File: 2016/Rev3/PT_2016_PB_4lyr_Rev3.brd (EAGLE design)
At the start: 155.7 x 202.7 mm, 170 parts, among them Q1 MOSFET-NCHANNELFDD8780, Q12 2N7002, Q3 MOSFET-NCHANNELFDD8780, Q4 MMBT2222A, Q5 MMBT4403

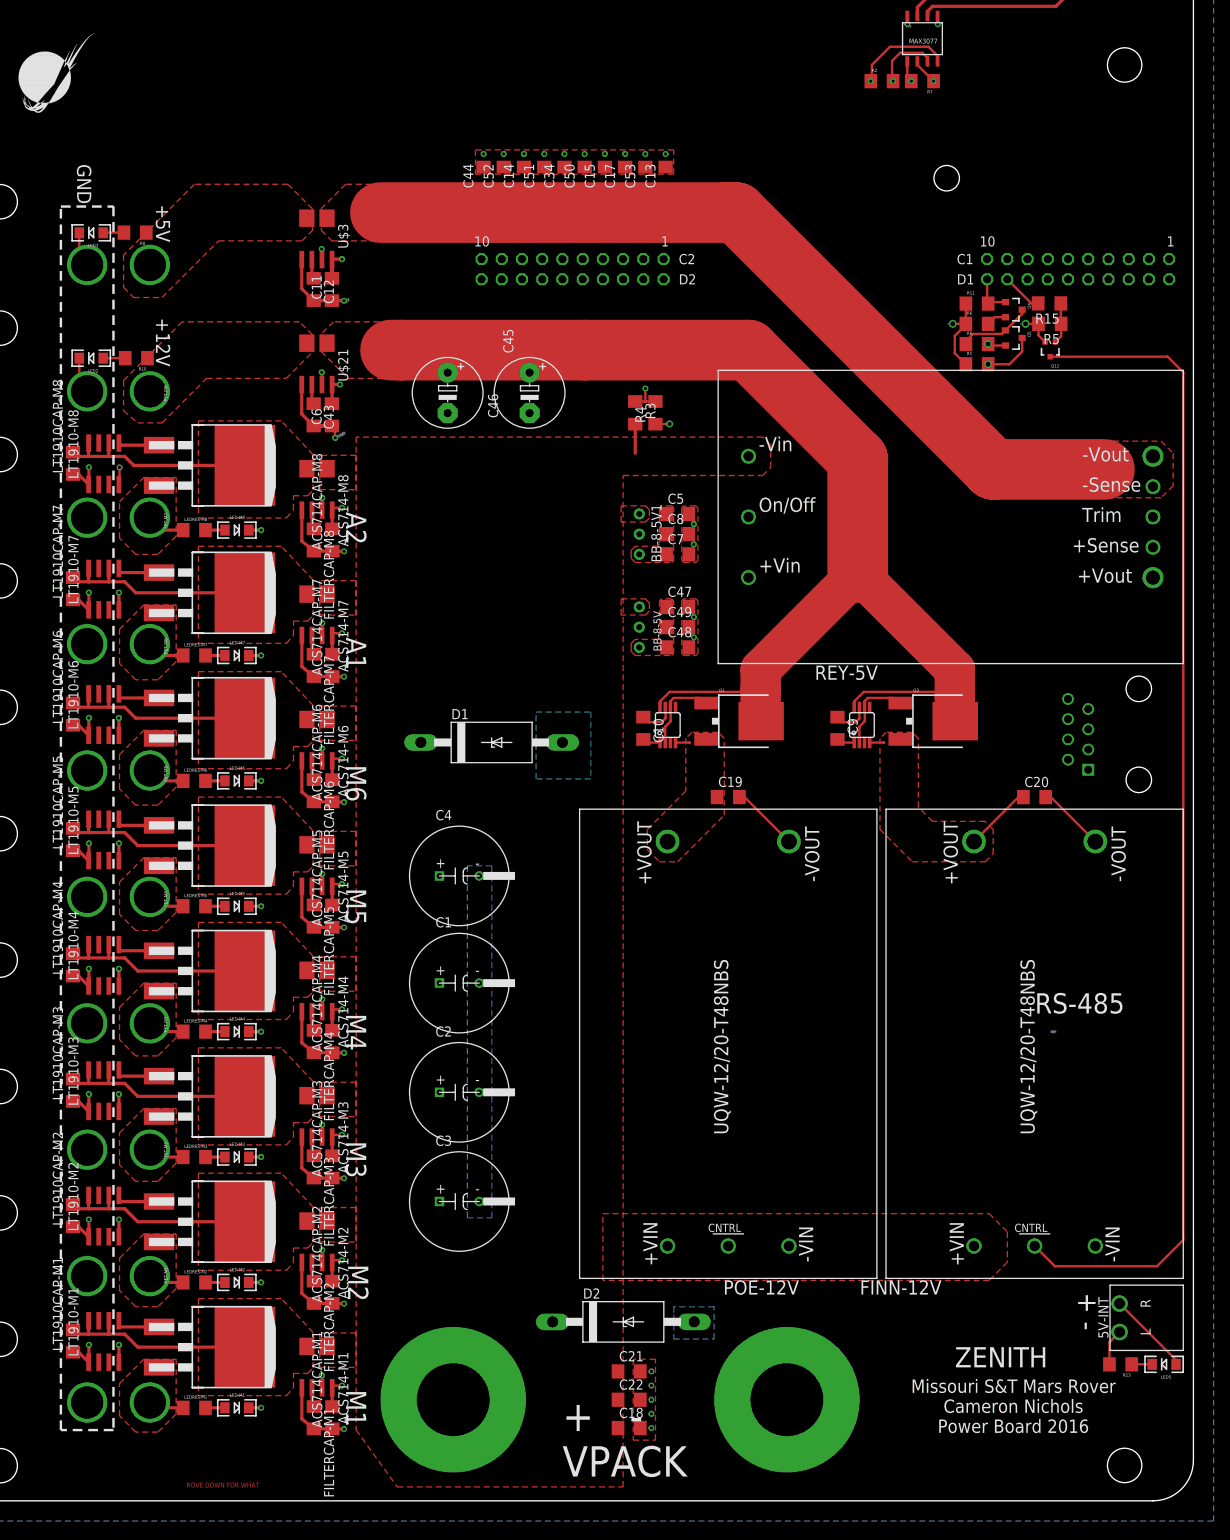
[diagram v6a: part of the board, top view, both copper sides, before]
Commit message: Changed 5V on/off circuit, enlarged planes
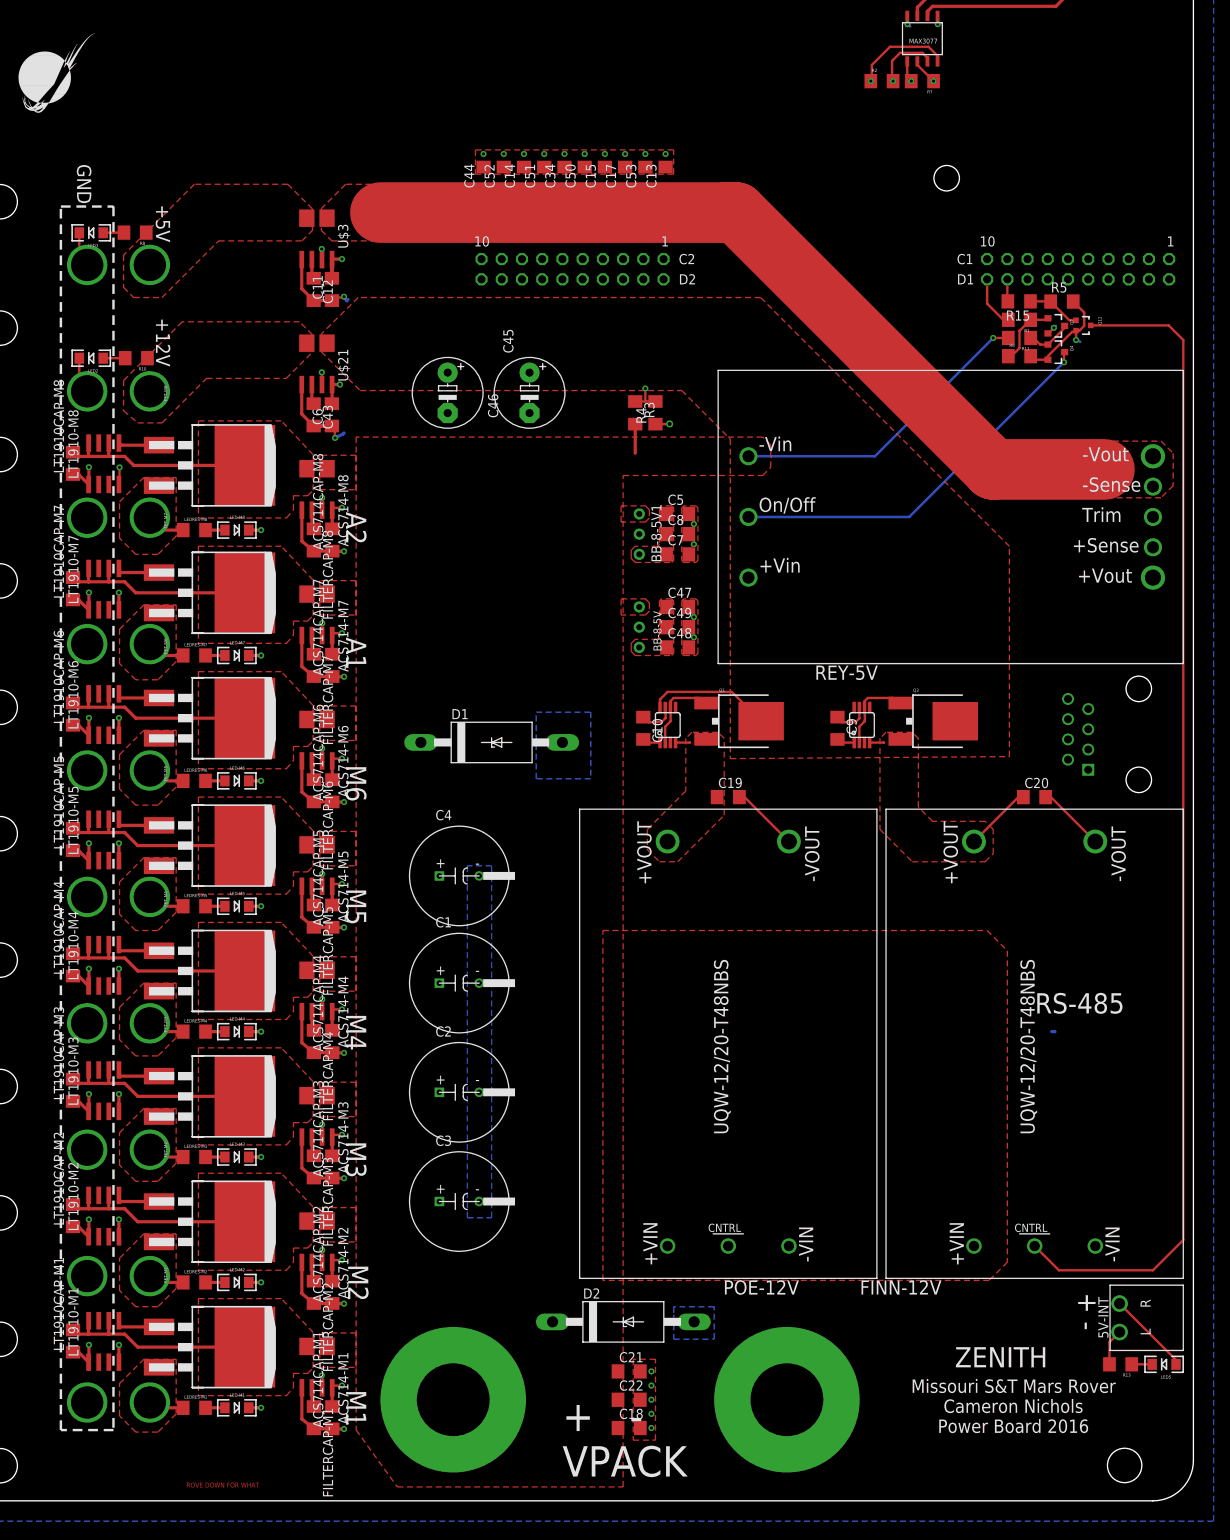
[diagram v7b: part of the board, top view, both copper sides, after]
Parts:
- removed Q5: MMBT4403, SparkFun-DiscreteSemi:SOT23-3
- removed R9: 1k, SparkFun-Passives:1206
- removed U$11: MOUNTING_HOLE#8, MRDT-Hardware:#8_SCREW
- added Q2: MMBT2222A, SparkFun-DiscreteSemi:SOT23-3
- R1, R11, R6: value 1k -> 100k
- moved R1 7.73 mm to (133.9, 148.3), turned to 180 degrees
- moved Q4 7.54 mm to (138.4, 144.3)
- moved R11 6.86 mm to (133.9, 146.1), turned to 180 degrees
- moved R6 6.71 mm to (133.9, 143.8)
- moved Q12 5.13 mm to (141.9, 147.6), turned to 270 degrees
- moved R15 3.82 mm to (133.8, 150.6)
- moved R5 3.18 mm to (139.2, 150.6), turned to 0 degrees
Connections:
- removed net N$43: Q5.3, R1.2, U$7.P$1
- new net N$14: Q2.1, R1.1, R6.1
- net GND: now also Q2.2, Q4.2, R6.2; no longer R1.1, R11.1, R6.1
- net N$11: now also U$7.P$1; no longer Q5.1, R9.1
- net N$15: now also Q2.3, Q4.1, R11.1; no longer Q4.2, R6.2
- net SIG-5V: now also R1.2; no longer Q4.1, R11.2
- net V_BATT: now also R11.2; no longer Q5.2, R9.2
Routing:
- net N$33: track 170.9 -> 15.6 mm
- net N$43: track 44.7 -> 0.00 mm, vias 1 -> 0
- net N$11: track 9.38 -> 49.0 mm, vias 0 -> 1
- net N$14: track 0.00 -> 8.21 mm
- net N$15: track 2.51 -> 5.74 mm
- net SIG-12V: track 5.13 -> 2.80 mm
- net GND: track 202.8 -> 201.1 mm
- net N$114: track 5.16 -> 6.70 mm
- net SIG-5V: track 5.35 -> 6.55 mm
- net N$4: track 188.0 -> 187.3 mm
- net V_BATT: track 41.8 -> 42.4 mm

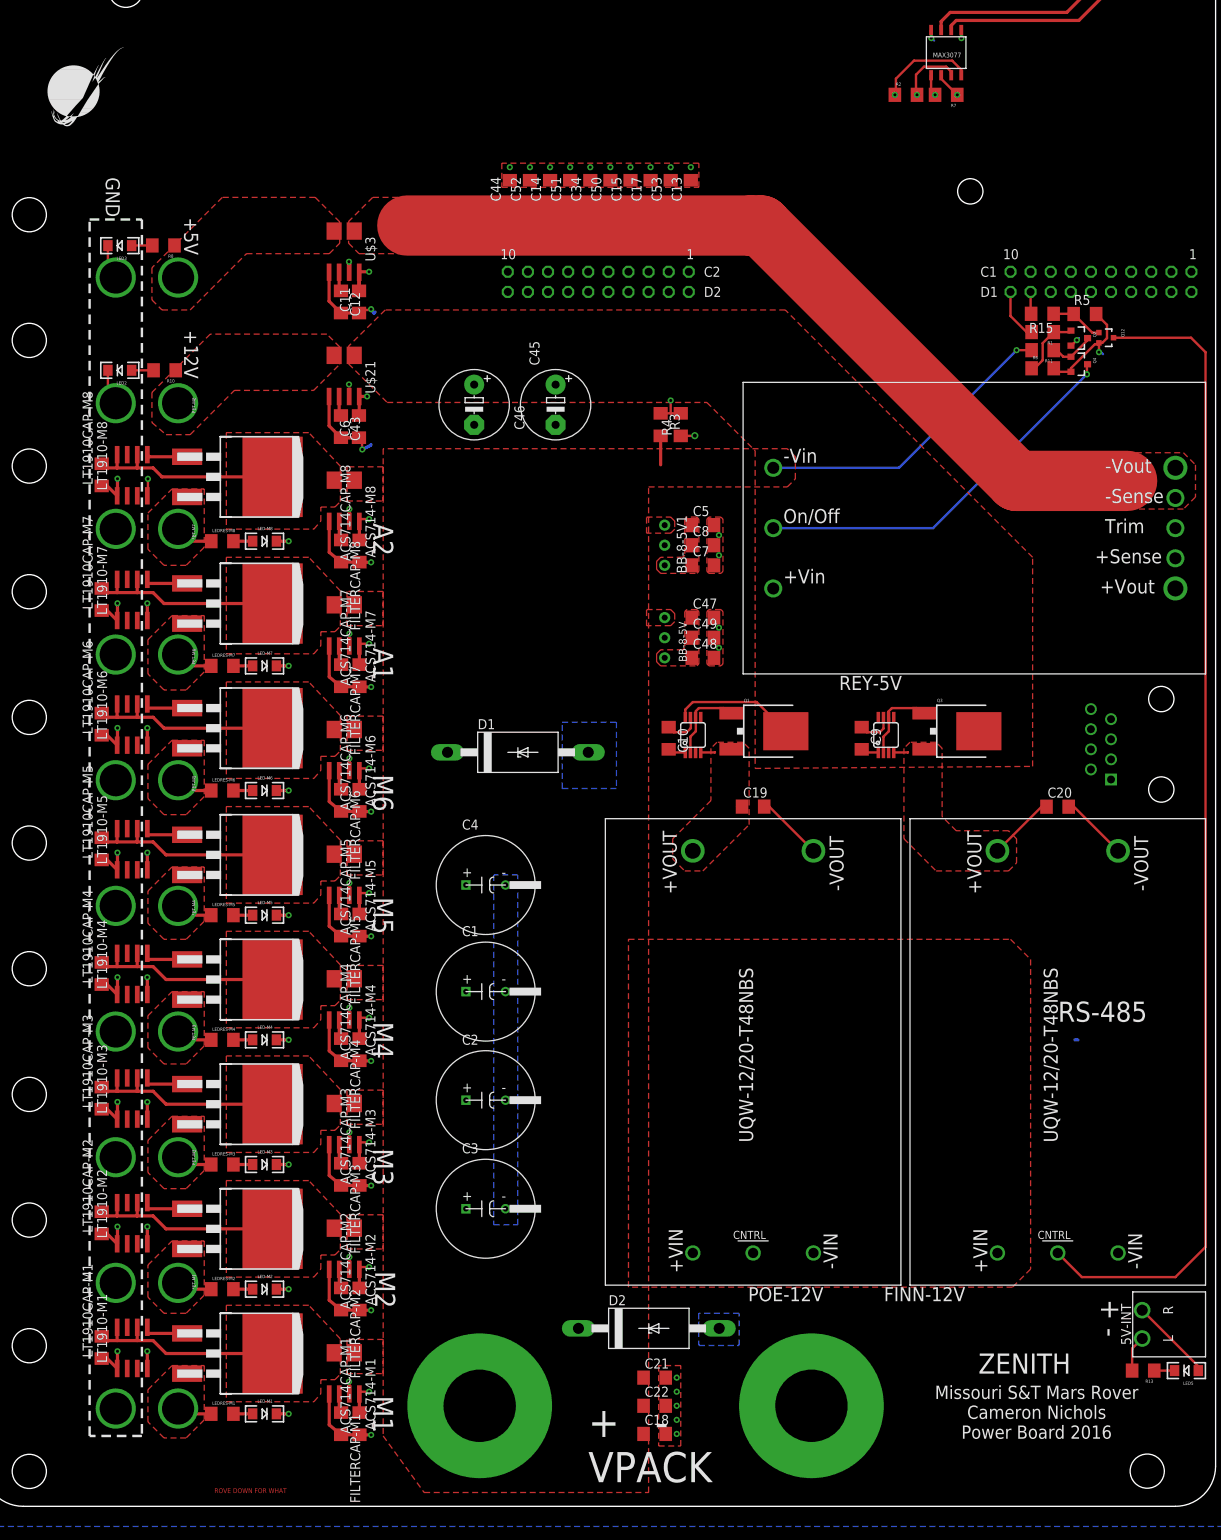
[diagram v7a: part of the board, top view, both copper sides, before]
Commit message: Cleaned up some routing/planes
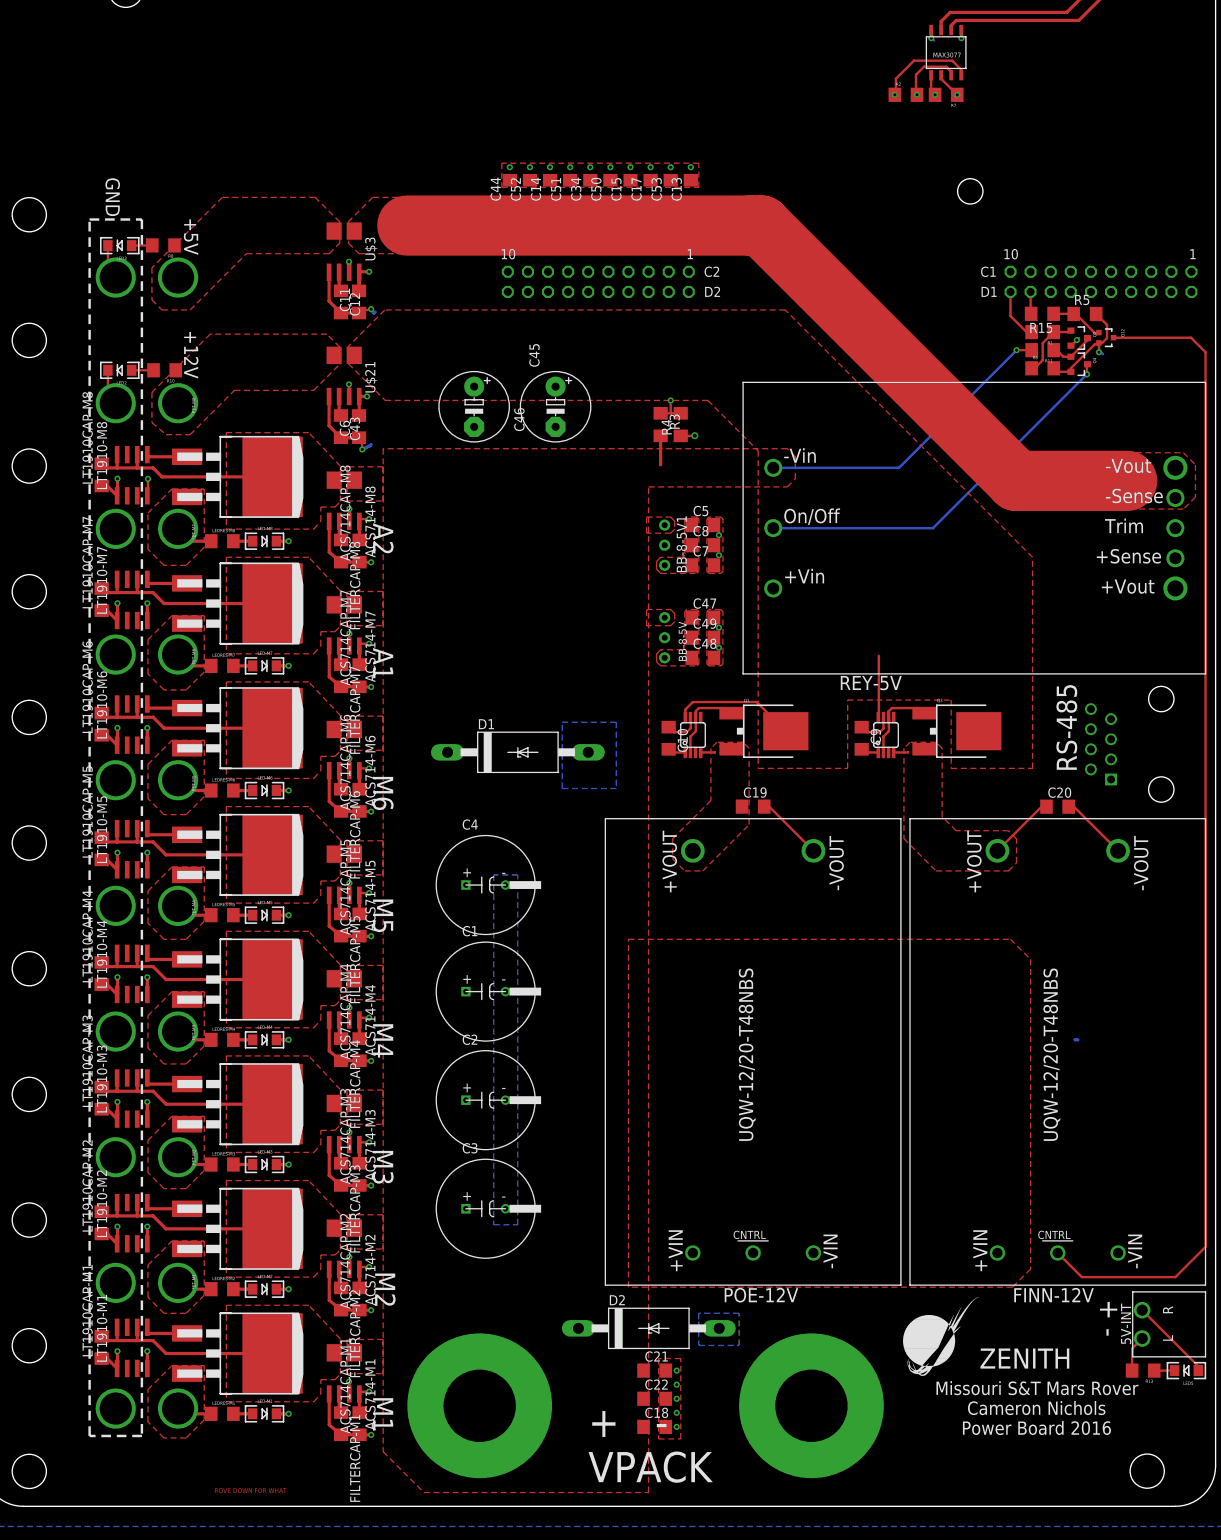
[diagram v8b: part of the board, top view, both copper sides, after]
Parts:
- R5: value 1k -> 100k
- moved U$22 191.3 mm to (116.2, 15.6)
- moved C22 0.89 mm to (84.8, 13.6)
- moved C18 0.89 mm to (84.8, 10.0)
- moved C21 0.89 mm to (84.8, 17.1)
- moved C45 0.25 mm to (72.3, 138.9)
- moved C46 0.25 mm to (62.0, 138.9)
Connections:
- removed net N$100: U$1.RST1, U$1.RST_2
- removed net N$101: U$1.PB2
- removed net N$102: U$1.PB3
- removed net N$110: U$1.PD5
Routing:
- net N$33: track 15.6 -> 23.5 mm
